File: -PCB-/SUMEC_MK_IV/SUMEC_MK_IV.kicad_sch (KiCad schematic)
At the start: 0 parts

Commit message: i did, something (archive return but now its better)
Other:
- added sheet CONNECTIVITY (CONNECTIVITY.kicad_sch)
- added sheet GRAPHICS (GRAPHICS.kicad_sch)
- added sheet MCU (MCU.kicad_sch)
- added sheet MECHANICS (MECHANICS.kicad_sch)
- added sheet MOTOR_CONTROL (MOTOR_CONTROL.kicad_sch)
- added sheet POWER_SUPPLY (POWER_SUPPLY.kicad_sch)
- added sheet SENSORS (SENSORS.kicad_sch)

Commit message: font warning in schematic
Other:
- note added: "If you see schematic in wierd different fonts: my default font is set as BAHNSCHRIFT"
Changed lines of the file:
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@@
 		(comment 4 "SUMEC MK IV aka SMD-V3 board")
+	)
+	(text "If you see schematic in wierd different fonts: my default font is set as BAHNSCHRIFT"
+		(exclude_from_sim no)
+		(at 147.32 41.91 0)
+		(effects
+			(font
+				(size 2 2)
+				(color 0 0 0 1)
+			)
+		)
 	)
 	(symbol

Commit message: connector agregation and minor changes
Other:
- removed sheet SENSORS
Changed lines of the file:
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@@
-	)
-	(sheet
-		(at 187.96 48.895)
-		(size 59.69 30.48)
-		(stroke
-			(width 0.1524)
-			(type solid)
-			(color 0 0 0 1)
-		)
-		(fill
-			(color 255 255 255 1.0000)
-		)
-		(property "Sheetname" "SENSORS"
-			(at 205.74 66.04 0)
-			(effects
-				(font
-					(size 4 4)
-					(color 0 0 0 1)
-				)
-				(justify left bottom)
-			)
-		)
-		(property "Sheetfile" "SENSORS.kicad_sch"
-			(at 187.96 79.9596 0)
-			(effects
-				(font
-					(size 1.27 1.27)
-					(color 0 0 0 1)
-				)
-				(justify left top)
-			)
-		)
-		(instances
-			(project "SUMEC_MK_IV"
-				(path "/900bd7ac-cdf9-4a2f-8b1f-2c21e3760046"
-					(page "4")
-				)
-			)
-		)
 	)
 	(sheet

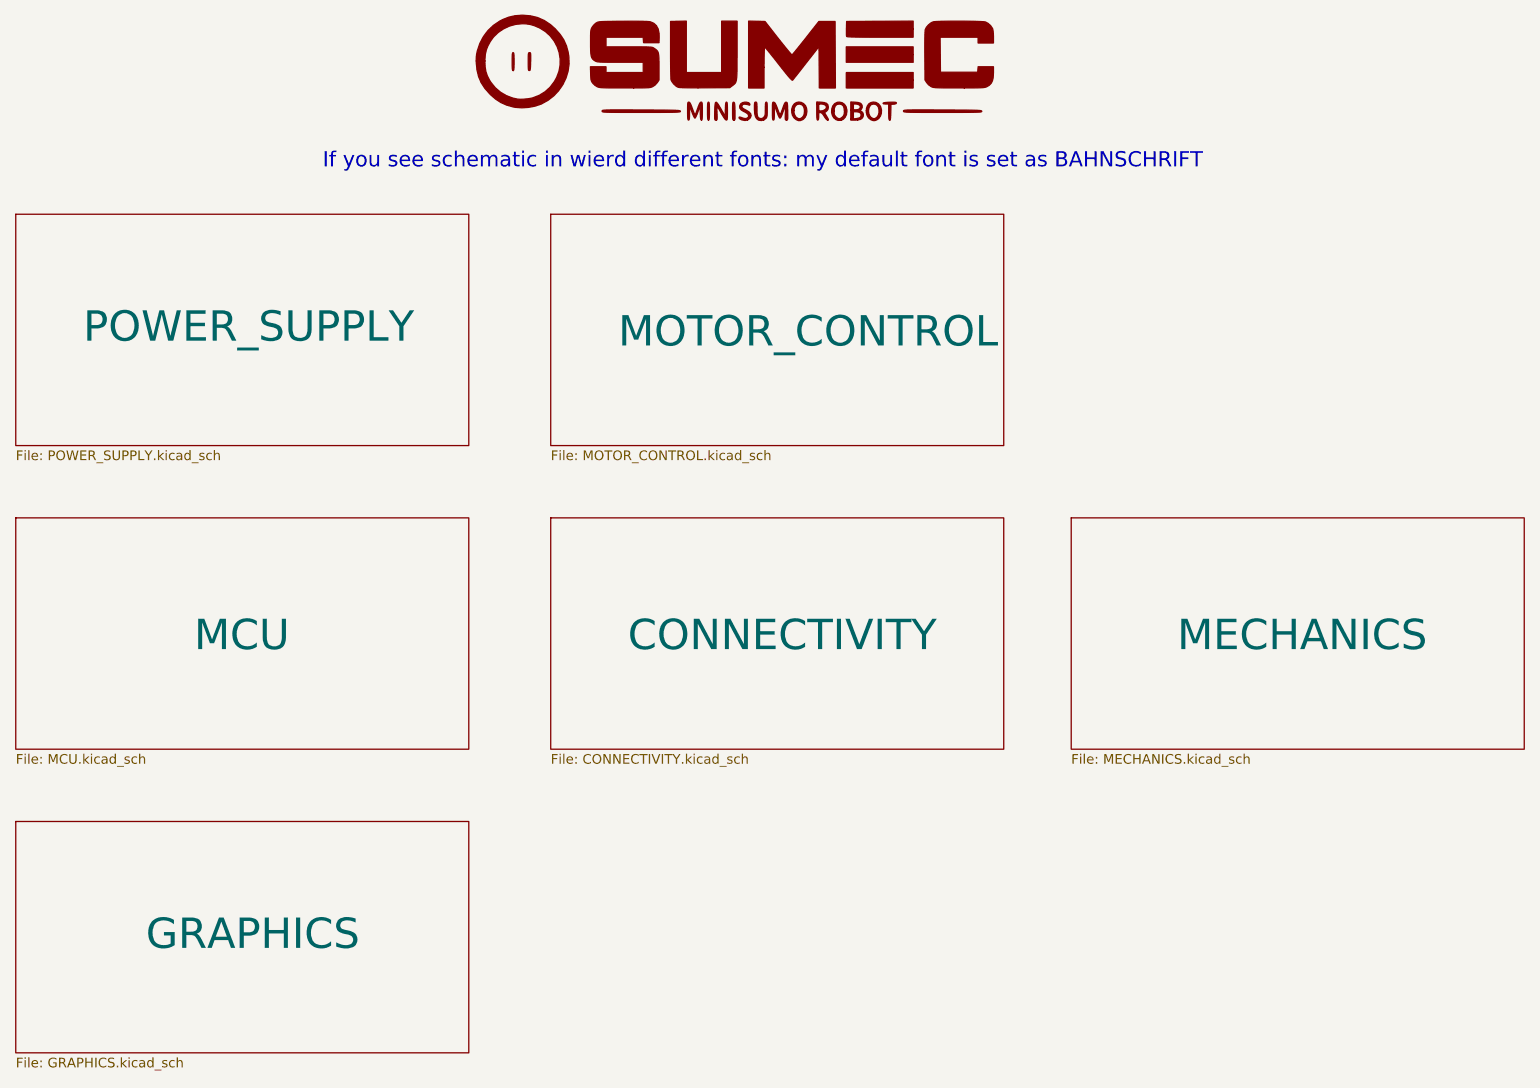
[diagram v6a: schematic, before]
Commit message: Schematic and PCB update
Schematic update:
- Font adjustment
- Block rearrangement

PCB update
- Silkscreen
- Minor layout update
- Graphic update
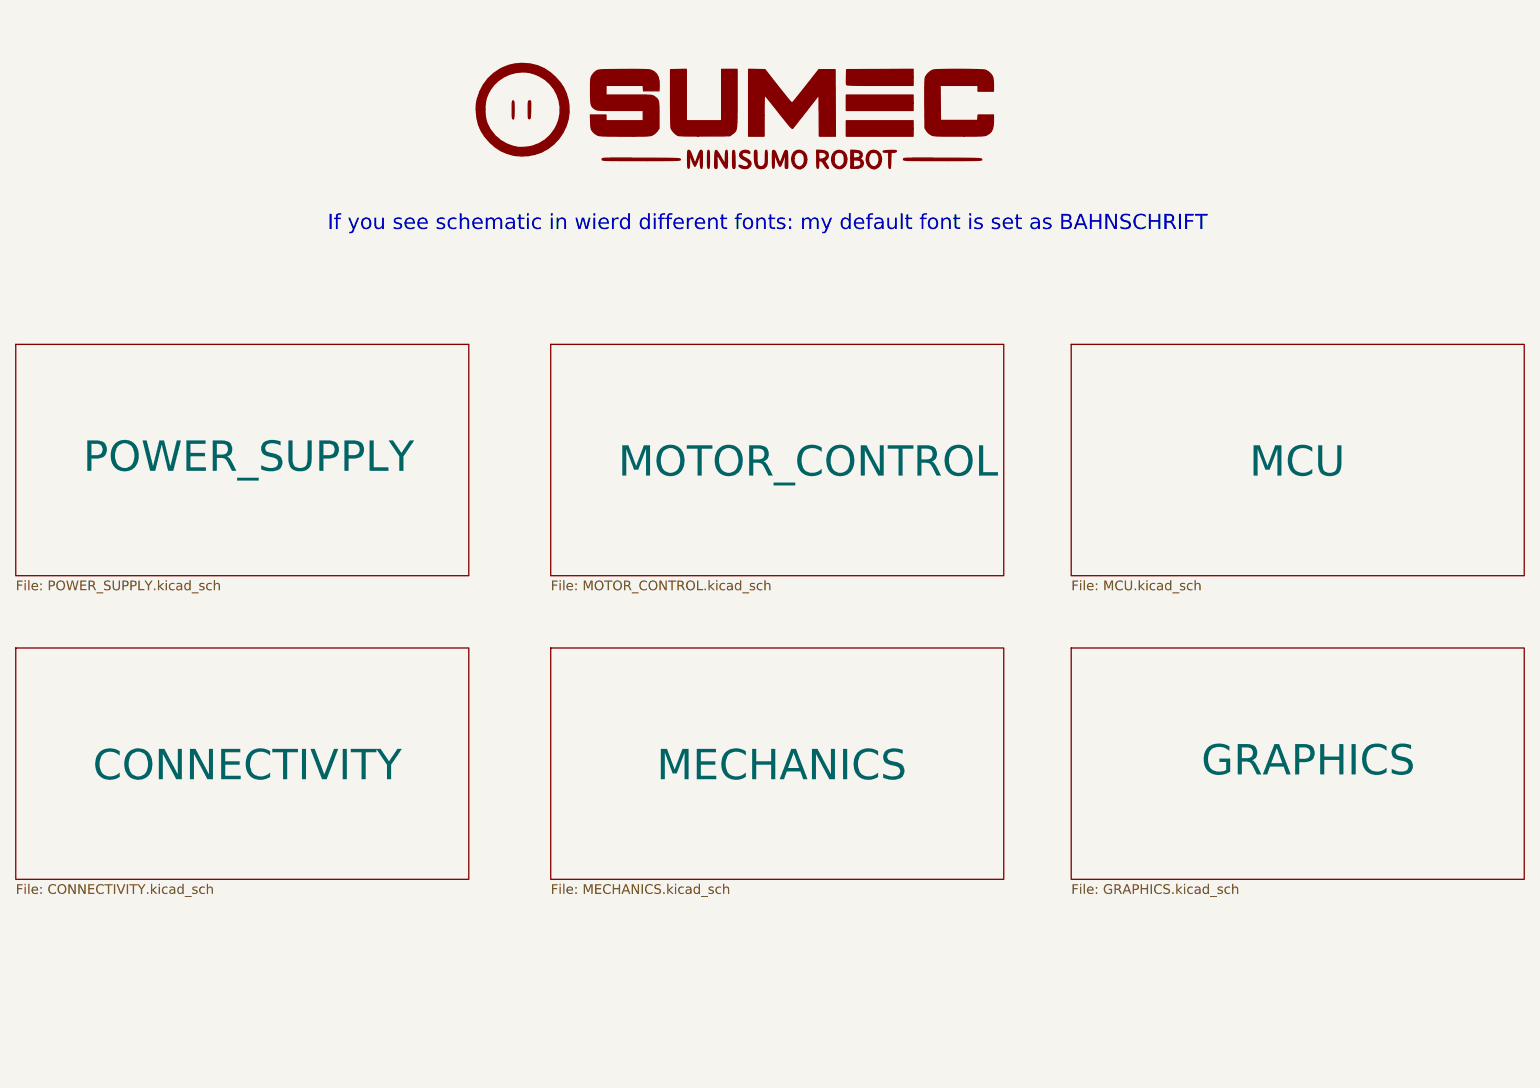
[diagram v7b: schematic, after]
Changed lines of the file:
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@@
 		(company "SPS NA PROSEKU")
 		(comment 1 "Made in Prague, Czech Republic")
-		(comment 2 "CONTACT: Savva Popov, menmenson09@gmail.com, +420 605 570 366")
-		(comment 3 "Made by Bismarx aka MenMenson")
+		(comment 2 "CONTACT: Savva Popov, savva.popov.sp@gmail.com, +420 605 570 366")
+		(comment 3 "Made by bismarx-v1")
 		(comment 4 "SUMEC MK IV aka SMD-V3 board")
 	)
 	(text "If you see schematic in wierd different fonts: my default font is set as BAHNSCHRIFT"
 		(exclude_from_sim no)
-		(at 147.32 41.91 0)
+		(at 147.955 50.165 0)
 		(effects
 			(font
+				(face "Bahnschrift")
 				(size 2 2)
 				(color 0 0 0 1)
@@
 	(symbol
 		(lib_id "sumec_sch_lib:LOGO SMALL")
-		(at 142.24 30.48 0)
+		(at 142.24 36.83 0)
 		(unit 1)
 		(exclude_from_sim no)
@@
 		(fields_autoplaced yes)
 		(property "Reference" "#G1"
-			(at 142.24 19.8543 0)
+			(at 142.24 26.2043 0)
 			(effects
 				(font
@@
 		)
 		(property "Value" "LOGO SMALL"
-			(at 142.24 41.1057 0)
+			(at 142.24 47.4557 0)
 			(effects
 				(font
@@
 		)
 		(property "Footprint" ""
-			(at 142.24 30.48 0)
+			(at 142.24 36.83 0)
 			(effects
 				(font
@@
 		)
 		(property "Datasheet" ""
-			(at 142.24 30.48 0)
+			(at 142.24 36.83 0)
 			(effects
 				(font
@@
 		)
 		(property "Description" ""
-			(at 142.24 30.48 0)
+			(at 142.24 36.83 0)
 			(effects
 				(font
@@
 	)
 	(sheet
-		(at 48.895 88.9)
+		(at 187.96 66.04)
 		(size 59.69 30.48)
 		(stroke
@@
 		)
 		(property "Sheetname" "MCU"
-			(at 72.39 106.68 0)
+			(at 211.455 83.82 0)
 			(effects
 				(font
@@
 		)
 		(property "Sheetfile" "MCU.kicad_sch"
-			(at 48.895 119.9646 0)
+			(at 187.96 97.1046 0)
 			(effects
 				(font
@@
 		)
 		(property "Field2" ""
-			(at 48.895 88.9 0)
+			(at 187.96 66.04 0)
 			(effects
 				(font
@@
 	)
 	(sheet
-		(at 119.38 48.895)
+		(at 119.38 66.04)
 		(size 59.69 30.48)
 		(stroke
@@
 		)
 		(property "Sheetname" "MOTOR_CONTROL"
-			(at 128.27 66.675 0)
+			(at 128.27 83.82 0)
 			(effects
 				(font
@@
 		)
 		(property "Sheetfile" "MOTOR_CONTROL.kicad_sch"
-			(at 119.38 79.9596 0)
+			(at 119.38 97.1046 0)
 			(effects
 				(font
@@
 	)
 	(sheet
-		(at 187.96 88.9)
+		(at 119.38 106.045)
 		(size 59.69 30.48)
 		(stroke
@@
 		)
 		(property "Sheetname" "MECHANICS"
-			(at 201.93 106.68 0)
-			(effects
-				(font
+			(at 133.35 123.825 0)
+			(effects
+				(font
+					(face "Bahnschrift")
 					(size 4 4)
 					(color 0 0 0 1)
@@
 		)
 		(property "Sheetfile" "MECHANICS.kicad_sch"
-			(at 187.96 119.9646 0)
+			(at 119.38 137.1096 0)
 			(effects
 				(font
@@
 	)
 	(sheet
-		(at 119.38 88.9)
+		(at 48.895 106.045)
 		(size 59.69 30.48)
 		(stroke
@@
 		)
 		(property "Sheetname" "CONNECTIVITY"
-			(at 129.54 106.68 0)
+			(at 59.055 123.825 0)
 			(effects
 				(font
@@
 		)
 		(property "Sheetfile" "CONNECTIVITY.kicad_sch"
-			(at 119.38 119.9646 0)
+			(at 48.895 137.1096 0)
 			(effects
 				(font
@@
 		)
 		(property "Field2" ""
-			(at 119.38 88.9 0)
+			(at 48.895 106.045 0)
 			(effects
 				(font
@@
 	)
 	(sheet
-		(at 48.895 48.895)
+		(at 48.895 66.04)
 		(size 59.69 30.48)
 		(stroke
@@
 		)
 		(property "Sheetname" "POWER_SUPPLY"
-			(at 57.785 66.04 0)
-			(effects
-				(font
+			(at 57.785 83.185 0)
+			(effects
+				(font
+					(face "Bahnschrift")
 					(size 4 4)
 					(color 0 0 0 1)
@@
 		)
 		(property "Sheetfile" "POWER_SUPPLY.kicad_sch"
-			(at 48.895 79.9596 0)
+			(at 48.895 97.1046 0)
 			(effects
 				(font
@@
 	)
 	(sheet
-		(at 48.895 128.905)
+		(at 187.96 106.045)
 		(size 59.69 30.48)
 		(stroke
@@
 		)
 		(property "Sheetname" "GRAPHICS"
-			(at 66.04 146.05 0)
-			(effects
-				(font
+			(at 205.105 123.19 0)
+			(effects
+				(font
+					(face "Bahnschrift")
 					(size 4 4)
 					(color 0 0 0 1)
@@
 		)
 		(property "Sheetfile" "GRAPHICS.kicad_sch"
-			(at 48.895 159.9696 0)
-			(effects
-				(font
+			(at 187.96 137.1096 0)
+			(effects
+				(font

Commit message: minor text changes
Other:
- note removed: "If you see schematic in wierd different fonts: my default font is set as BAHNSCHRIFT"
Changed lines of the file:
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@@
 		(comment 4 "SUMEC MK IV aka SMD-V3 board")
-	)
-	(text "If you see schematic in wierd different fonts: my default font is set as BAHNSCHRIFT"
-		(exclude_from_sim no)
-		(at 147.955 50.165 0)
-		(effects
-			(font
-				(face "Bahnschrift")
-				(size 2 2)
-				(color 0 0 0 1)
-			)
-		)
 	)
 	(symbol
